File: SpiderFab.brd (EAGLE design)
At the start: 69.8 x 50.8 mm, 47 parts, among them IC1 SN754410, J14 5.5x2.1mm Barrel, U1 ATMEGA328, U3 MCP73831, X1 USBSMD, Y1 16MHz

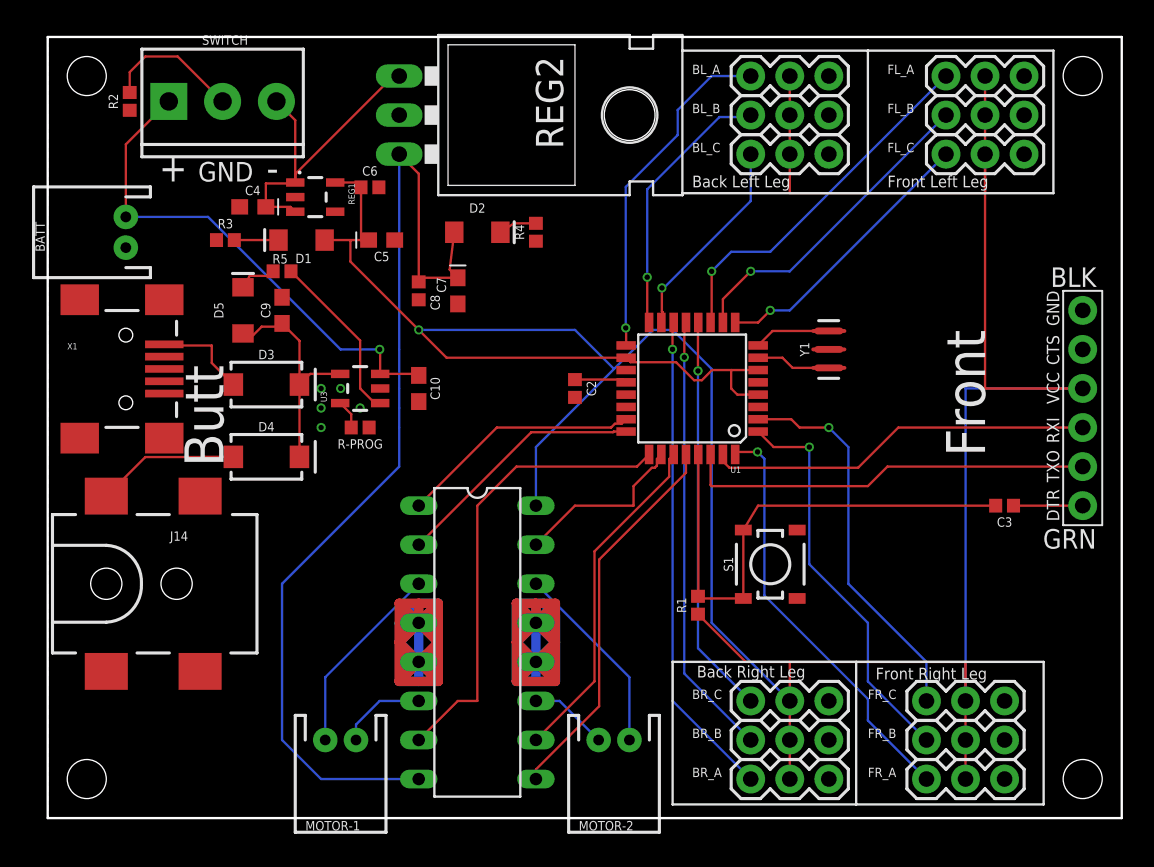
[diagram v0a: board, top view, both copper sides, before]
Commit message: Make power traces thicker.
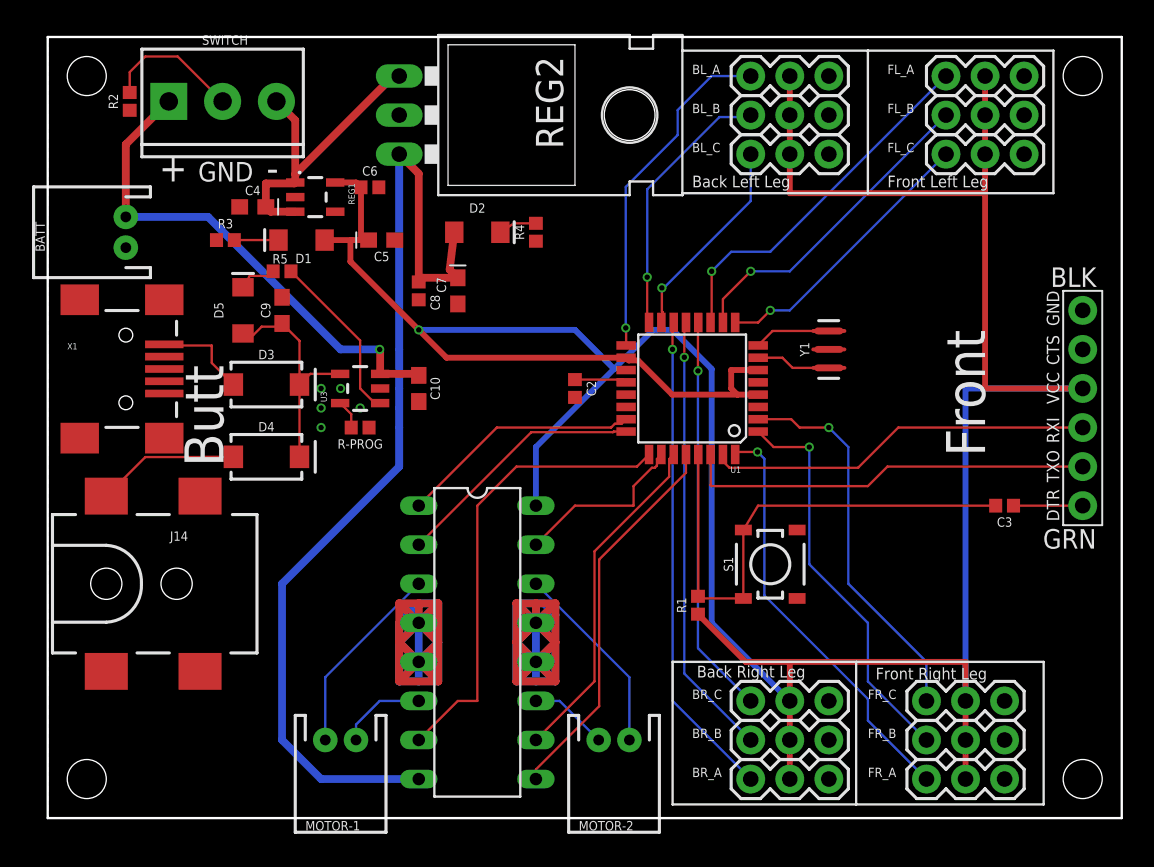
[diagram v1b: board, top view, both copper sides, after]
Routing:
- net VCC: track 210.9 -> 211.4 mm
